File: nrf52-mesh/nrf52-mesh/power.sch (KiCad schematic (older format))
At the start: 17 parts, among them U2 MAX1555, U4 TPS560200

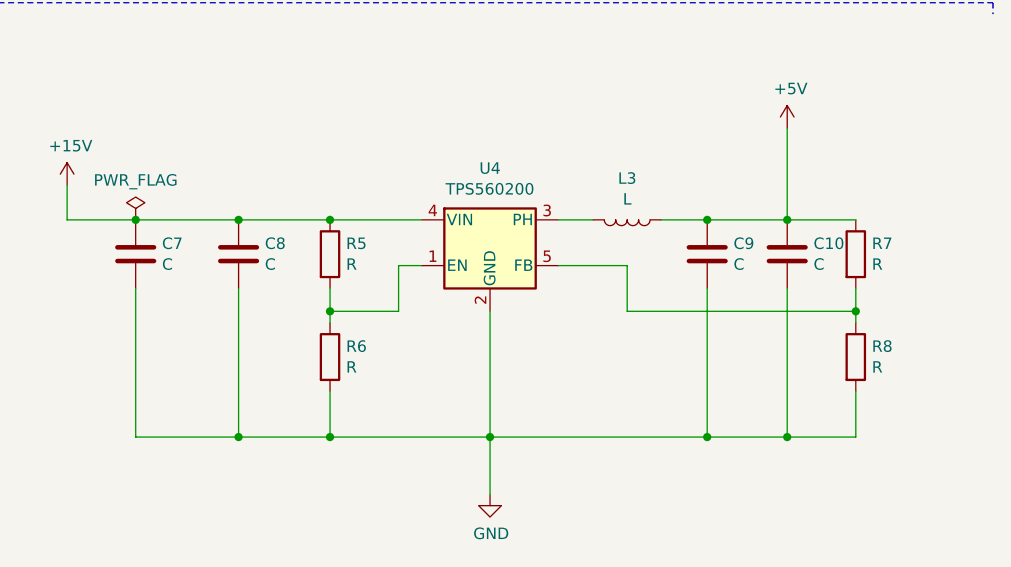
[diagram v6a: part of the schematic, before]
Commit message: CP2102N + MAX1555 + FAN5341 + TPS560200 + TLV62568
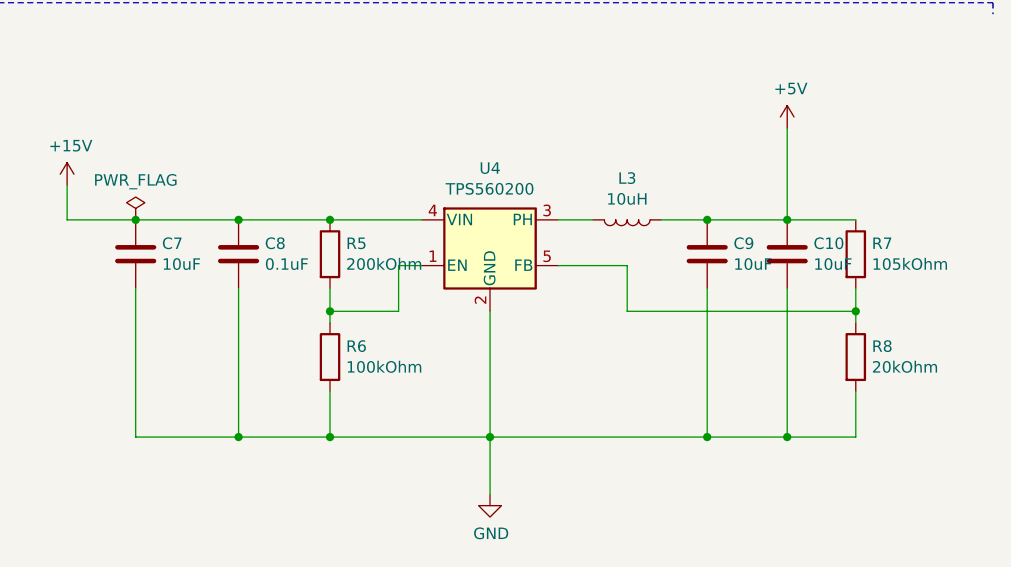
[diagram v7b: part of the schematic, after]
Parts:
- C1, C4: footprint Resistor_SMD:R_0402_1005Metric -> Capacitor_SMD:C_0402_1005Metric
- C10, C7, C9: value C -> 10uF; footprint (none) -> Capacitor_SMD:C_0603_1608Metric
- C8: value C -> 0.1uF; footprint (none) -> Capacitor_SMD:C_0402_1005Metric
- L3: value L -> 10uH; footprint (none) -> Inductor_SMD:L_0805_2012Metric
- R5: value R -> 200kOhm; footprint (none) -> Resistor_SMD:R_0402_1005Metric
- R6: value R -> 100kOhm; footprint (none) -> Resistor_SMD:R_0402_1005Metric
- R7: value R -> 105kOhm; footprint (none) -> Resistor_SMD:R_0402_1005Metric
- R8: value R -> 20kOhm; footprint (none) -> Resistor_SMD:R_0402_1005Metric
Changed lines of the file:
@@
 P 6950 4750
 F 0 "C7" H 7065 4796 50  0000 L CNN
-F 1 "C" H 7065 4705 50  0000 L CNN
-F 2 "" H 6988 4600 50  0001 C CNN
+F 1 "10uF" H 7065 4705 50  0000 L CNN
+F 2 "Capacitor_SMD:C_0603_1608Metric" H 6988 4600 50  0001 C CNN
 F 3 "~" H 6950 4750 50  0001 C CNN
 	1    6950 4750
@@
 P 7400 4750
 F 0 "C8" H 7515 4796 50  0000 L CNN
-F 1 "C" H 7515 4705 50  0000 L CNN
-F 2 "" H 7438 4600 50  0001 C CNN
+F 1 "0.1uF" H 7515 4705 50  0000 L CNN
+F 2 "Capacitor_SMD:C_0402_1005Metric" H 7438 4600 50  0001 C CNN
 F 3 "~" H 7400 4750 50  0001 C CNN
 	1    7400 4750
@@
 P 7800 4750
 F 0 "R5" H 7870 4796 50  0000 L CNN
-F 1 "R" H 7870 4705 50  0000 L CNN
-F 2 "" V 7730 4750 50  0001 C CNN
+F 1 "200kOhm" H 7870 4705 50  0000 L CNN
+F 2 "Resistor_SMD:R_0402_1005Metric" V 7730 4750 50  0001 C CNN
 F 3 "~" H 7800 4750 50  0001 C CNN
 	1    7800 4750
@@
 P 7800 5200
 F 0 "R6" H 7870 5246 50  0000 L CNN
-F 1 "R" H 7870 5155 50  0000 L CNN
-F 2 "" V 7730 5200 50  0001 C CNN
+F 1 "100kOhm" H 7870 5155 50  0000 L CNN
+F 2 "Resistor_SMD:R_0402_1005Metric" V 7730 5200 50  0001 C CNN
 F 3 "~" H 7800 5200 50  0001 C CNN
 	1    7800 5200
@@
 P 9100 4600
 F 0 "L3" V 8919 4600 50  0000 C CNN
-F 1 "L" V 9010 4600 50  0000 C CNN
-F 2 "" H 9100 4600 50  0001 C CNN
+F 1 "10uH" V 9010 4600 50  0000 C CNN
+F 2 "Inductor_SMD:L_0805_2012Metric" H 9100 4600 50  0001 C CNN
 F 3 "~" H 9100 4600 50  0001 C CNN
 	1    9100 4600
@@
 P 9450 4750
 F 0 "C9" H 9565 4796 50  0000 L CNN
-F 1 "C" H 9565 4705 50  0000 L CNN
-F 2 "" H 9488 4600 50  0001 C CNN
+F 1 "10uF" H 9565 4705 50  0000 L CNN
+F 2 "Capacitor_SMD:C_0603_1608Metric" H 9488 4600 50  0001 C CNN
 F 3 "~" H 9450 4750 50  0001 C CNN
 	1    9450 4750
@@
 P 9800 4750
 F 0 "C10" H 9915 4796 50  0000 L CNN
-F 1 "C" H 9915 4705 50  0000 L CNN
-F 2 "" H 9838 4600 50  0001 C CNN
+F 1 "10uF" H 9915 4705 50  0000 L CNN
+F 2 "Capacitor_SMD:C_0603_1608Metric" H 9838 4600 50  0001 C CNN
 F 3 "~" H 9800 4750 50  0001 C CNN
 	1    9800 4750
@@
 P 10100 4750
 F 0 "R7" H 10170 4796 50  0000 L CNN
-F 1 "R" H 10170 4705 50  0000 L CNN
-F 2 "" V 10030 4750 50  0001 C CNN
+F 1 "105kOhm" H 10170 4705 50  0000 L CNN
+F 2 "Resistor_SMD:R_0402_1005Metric" V 10030 4750 50  0001 C CNN
 F 3 "~" H 10100 4750 50  0001 C CNN
 	1    10100 4750
@@
 P 10100 5200
 F 0 "R8" H 10170 5246 50  0000 L CNN
-F 1 "R" H 10170 5155 50  0000 L CNN
-F 2 "" V 10030 5200 50  0001 C CNN
+F 1 "20kOhm" H 10170 5155 50  0000 L CNN
+F 2 "Resistor_SMD:R_0402_1005Metric" V 10030 5200 50  0001 C CNN
 F 3 "~" H 10100 5200 50  0001 C CNN
 	1    10100 5200
@@
 F 0 "C1" H 1165 4996 50  0000 L CNN
 F 1 "1uF" H 1165 4905 50  0000 L CNN
-F 2 "Resistor_SMD:R_0402_1005Metric" H 1088 4800 50  0001 C CNN
+F 2 "Capacitor_SMD:C_0402_1005Metric" H 1088 4800 50  0001 C CNN
 F 3 "~" H 1050 4950 50  0001 C CNN
 	1    1050 4950
@@
 F 0 "C4" H 2235 5204 50  0000 R CNN
 F 1 "1uF" H 2235 5295 50  0000 R CNN
-F 2 "Resistor_SMD:R_0402_1005Metric" H 2388 5100 50  0001 C CNN
+F 2 "Capacitor_SMD:C_0402_1005Metric" H 2388 5100 50  0001 C CNN
 F 3 "~" H 2350 5250 50  0001 C CNN
 	1    2350 5250

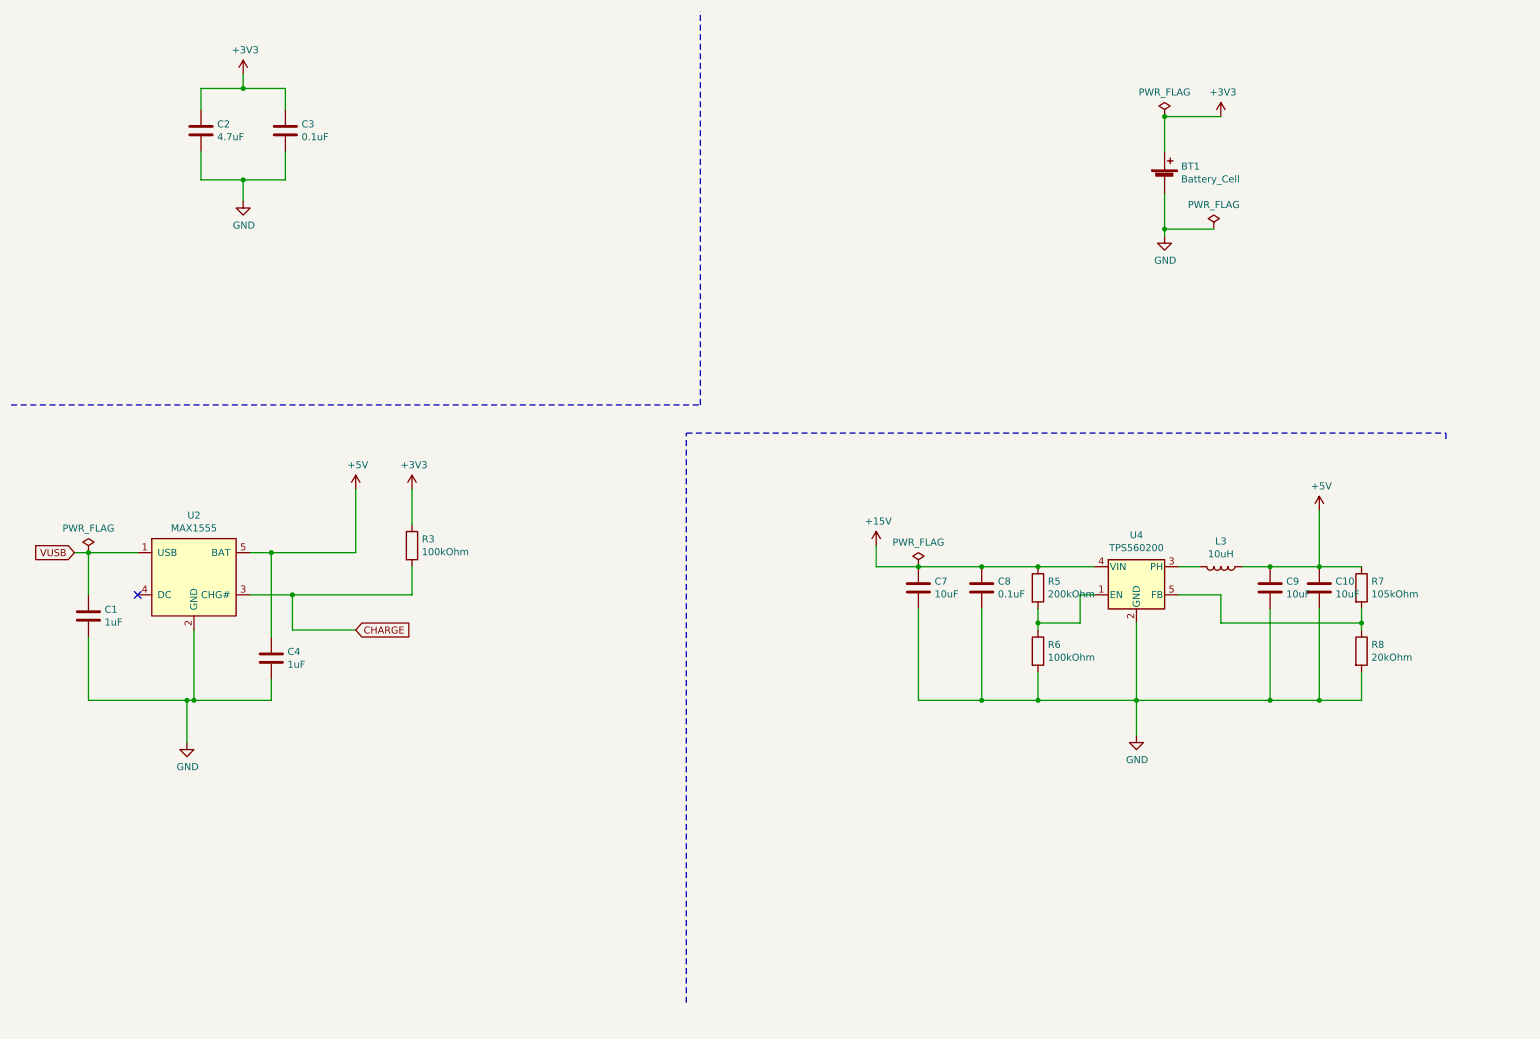
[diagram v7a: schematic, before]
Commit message: nRF52 + ESP WROOM
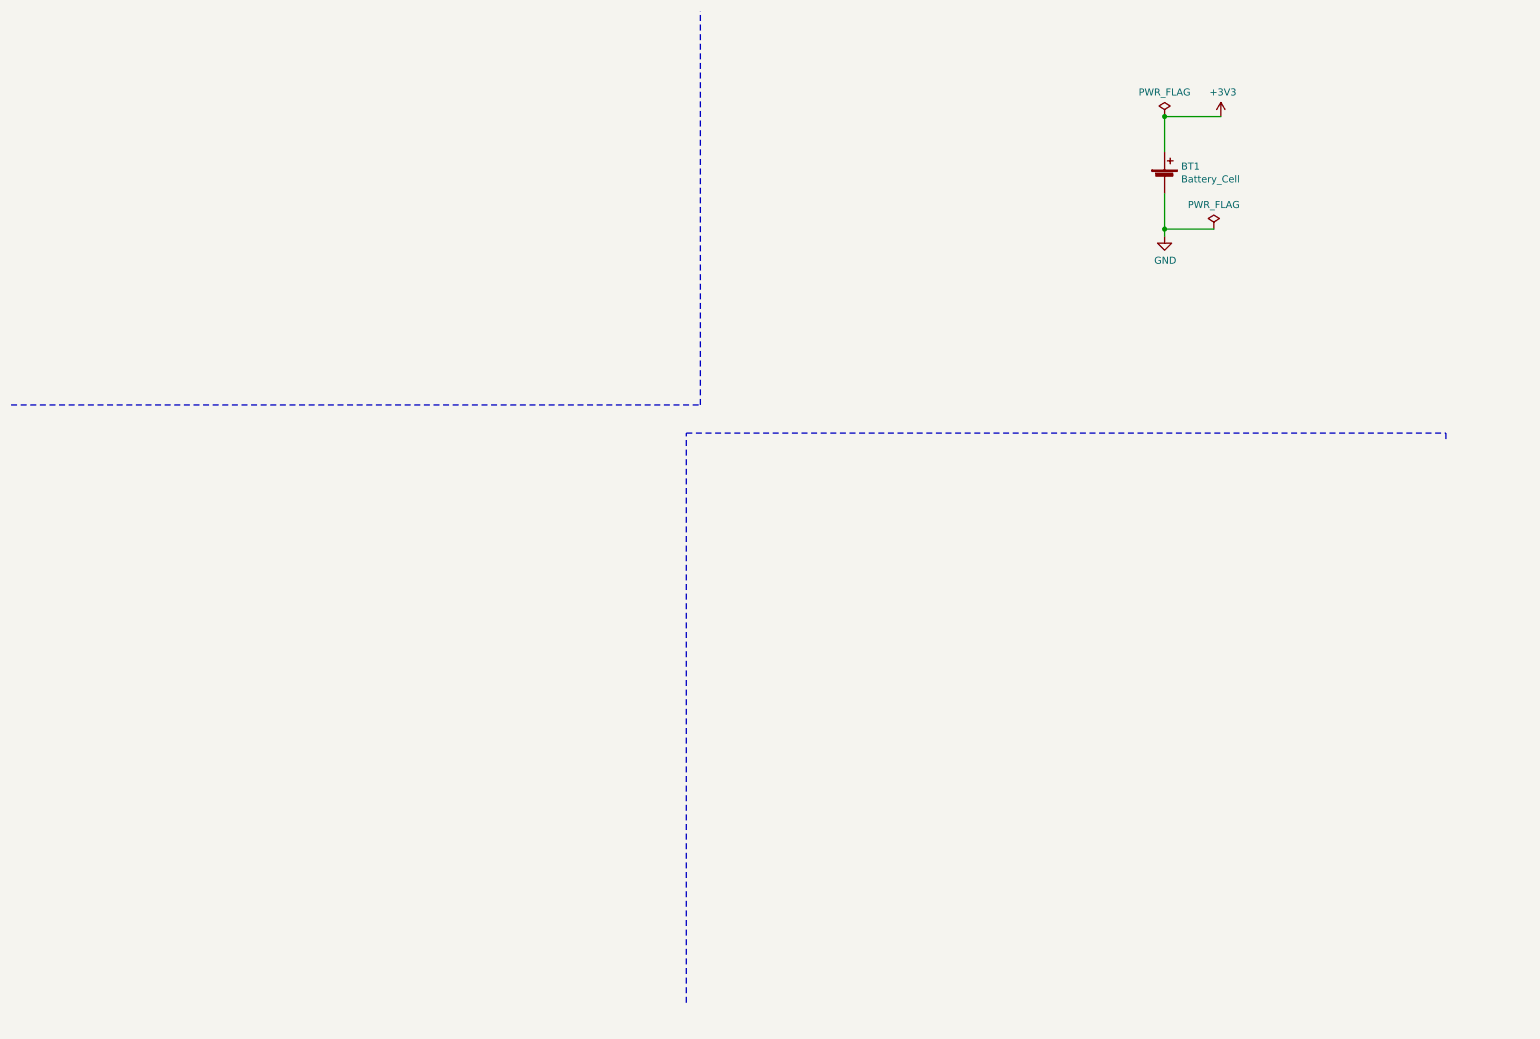
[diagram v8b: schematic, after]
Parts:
- removed C1, C4: 1uF, Capacitor_SMD:C_0402_1005Metric, symbol Device:C
- removed C10, C7, C9: 10uF, Capacitor_SMD:C_0603_1608Metric, symbol Device:C
- removed C2: 4.7uF, Capacitor_SMD:C_0402_1005Metric, symbol Device:C
- removed C3, C8: 0.1uF, Capacitor_SMD:C_0402_1005Metric, symbol Device:C
- removed L3: 10uH, Inductor_SMD:L_0805_2012Metric, symbol Device:L
- removed R3, R6: 100kOhm, Resistor_SMD:R_0402_1005Metric, symbol Device:R
- removed R5: 200kOhm, Resistor_SMD:R_0402_1005Metric, symbol Device:R
- removed R7: 105kOhm, Resistor_SMD:R_0402_1005Metric, symbol Device:R
- removed R8: 20kOhm, Resistor_SMD:R_0402_1005Metric, symbol Device:R
- removed U2: MAX1555, Package_TO_SOT_SMD:SOT-23-5, symbol kilib:MAX1555
- removed U4: TPS560200, Package_TO_SOT_SMD:SOT-23-5, symbol Regulator_Switching:TPS560200
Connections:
- no-connect marks 1 -> 0
